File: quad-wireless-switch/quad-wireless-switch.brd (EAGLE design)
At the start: 38.1 x 108 mm, 78 parts, among them IC1 LM2937IMP-3.3, Q1 DN2625K4-G, Q2 SI2323DS-T1-E3, Q3 IRL520, Q4 IRL520, Q5 IRL520, Q6 IRL520, U2 SDB501

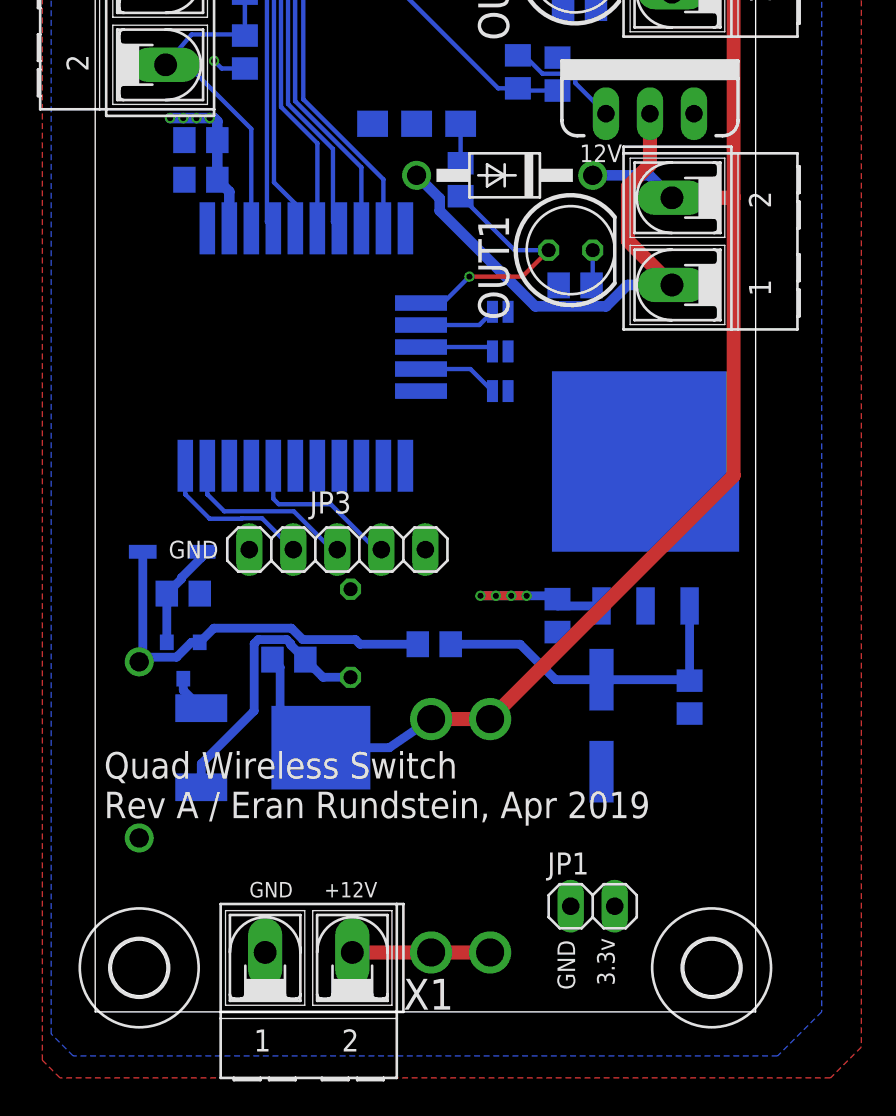
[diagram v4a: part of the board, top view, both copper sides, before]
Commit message: quad-wireless-switch
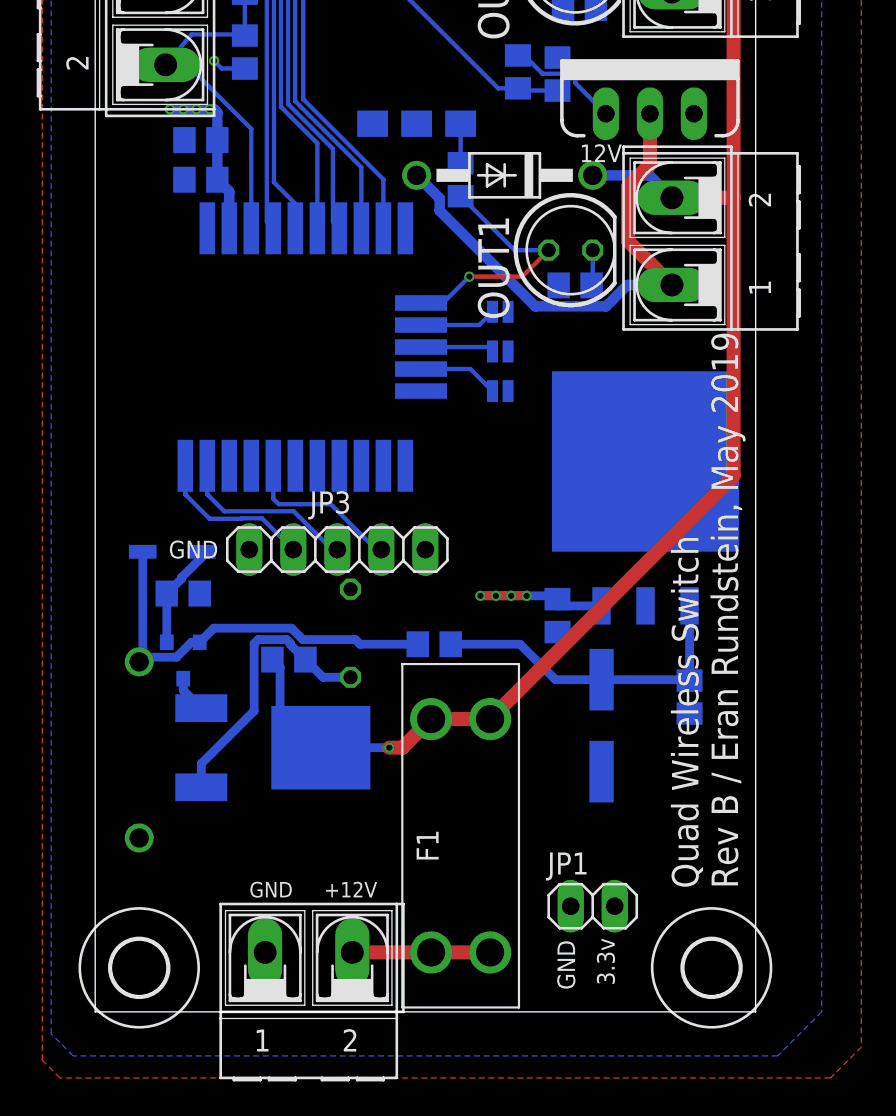
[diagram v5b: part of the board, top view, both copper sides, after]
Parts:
- flipped F1 to the top
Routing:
- net 3.3V: track 27.6 -> 28.1 mm
- net 12V: track 167.2 -> 167.4 mm, vias 3 -> 4
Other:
- board text added: "Quad Wireless Switch Rev B / Eran Rundstein, May 2019"
- board text removed: "Quad Wireless Switch Rev A / Eran Rundstein, Apr 2019"
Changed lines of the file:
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@@
 <wire x1="38.1" y1="107.95" x2="0" y2="107.95" width="0" layer="20"/>
 <wire x1="0" y1="107.95" x2="0" y2="0" width="0" layer="20"/>
-<text x="0.508" y="11.176" size="1.524" layer="25">Quad Wireless Switch
-Rev A / Eran Rundstein, Apr 2019</text>
+<text x="37.084" y="7.112" size="1.524" layer="25" rot="R90">Quad Wireless Switch
+Rev B / Eran Rundstein, May 2019</text>
 <text x="13.208" y="6.604" size="0.889" layer="25">+12V</text>
 <text x="8.89" y="6.604" size="0.889" layer="25">GND</text>
@@
 <attribute name="MF" value="" x="12.319" y="3.429" size="1.778" layer="27" display="off"/>
 <attribute name="MPN" value="" x="12.319" y="3.429" size="1.778" layer="27" display="off"/>
-<attribute name="NAME" x="17.78" y="0.127" size="1.778" layer="25"/>
 <attribute name="OC_FARNELL" value="unknown" x="12.319" y="3.429" size="1.778" layer="27" display="off"/>
 <attribute name="OC_NEWARK" value="unknown" x="12.319" y="3.429" size="1.778" layer="27" display="off"/>
 <attribute name="VALUE" x="9.144" y="-2.286" size="1.778" layer="27"/>
 </element>
-<element name="F1" library="keves-ng" library_urn="urn:adsk.eagle:library:1429743" package="KEYSTONE-3557-2" package3d_urn="urn:adsk.eagle:package:1429787/2" value="KEYSTONE-3557-2" x="21.082" y="10.16" smashed="yes" rot="MR90">
-<attribute name="NAME" x="22.352" y="8.636" size="1.27" layer="26" rot="MR90"/>
+<element name="F1" library="keves-ng" library_urn="urn:adsk.eagle:library:1429743" package="KEYSTONE-3557-2" package3d_urn="urn:adsk.eagle:package:1429787/2" value="KEYSTONE-3557-2" x="21.082" y="10.16" smashed="yes" rot="R90">
+<attribute name="NAME" x="19.812" y="8.636" size="1.27" layer="25" rot="R90"/>
 </element>
 <element name="Q1" library="SparkFun-DiscreteSemi" package="DPAK" value="DN2625K4-G" x="11.43" y="15.24" smashed="yes" rot="MR90">
@@
 <wire x1="7.736" y1="47.316" x2="7.046" y2="48.006" width="0.6096" layer="16"/>
 <wire x1="7.046" y1="48.006" x2="7.046" y2="50.292" width="0.6096" layer="16"/>
-<wire x1="7.046" y1="50.292" x2="7.046" y2="51.374" width="0.6096" layer="16"/>
-<wire x1="7.046" y1="51.374" x2="6.858" y2="51.562" width="0.6096" layer="16"/>
-<wire x1="6.858" y1="51.562" x2="6.604" y2="51.562" width="0.6096" layer="16"/>
-<wire x1="6.604" y1="51.562" x2="5.842" y2="51.562" width="0.6096" layer="16"/>
-<wire x1="5.842" y1="51.562" x2="5.08" y2="51.562" width="0.6096" layer="16"/>
-<wire x1="5.08" y1="51.562" x2="4.318" y2="51.562" width="0.6096" layer="16"/>
-<via x="4.318" y="51.562" extent="1-16" drill="0.35"/>
-<via x="5.08" y="51.562" extent="1-16" drill="0.35"/>
-<via x="5.842" y="51.562" extent="1-16" drill="0.35"/>
-<via x="6.604" y="51.562" extent="1-16" drill="0.35"/>
+<wire x1="7.046" y1="50.292" x2="7.046" y2="51.882" width="0.6096" layer="16"/>
+<wire x1="7.046" y1="51.882" x2="6.858" y2="52.07" width="0.6096" layer="16"/>
+<wire x1="6.858" y1="52.07" x2="6.604" y2="52.07" width="0.6096" layer="16"/>
+<wire x1="6.604" y1="52.07" x2="5.842" y2="52.07" width="0.6096" layer="16"/>
+<wire x1="5.842" y1="52.07" x2="5.08" y2="52.07" width="0.6096" layer="16"/>
+<wire x1="5.08" y1="52.07" x2="4.318" y2="52.07" width="0.6096" layer="16"/>
+<via x="4.318" y="52.07" extent="1-16" drill="0.35"/>
+<via x="5.08" y="52.07" extent="1-16" drill="0.35"/>
+<via x="5.842" y="52.07" extent="1-16" drill="0.35"/>
+<via x="6.604" y="52.07" extent="1-16" drill="0.35"/>
 <contactref element="JP1" pad="2"/>
 </signal>
@@
 <contactref element="R1" pad="2"/>
 <contactref element="OUT1" pad="2"/>
-<wire x1="19.3802" y1="16.891" x2="16.9672" y2="15.24" width="0.508" layer="16"/>
 <wire x1="16.9672" y1="15.24" x2="13.018" y2="15.24" width="0.508" layer="16"/>
 <wire x1="10.226" y1="20.32" x2="10.668" y2="19.878" width="0.508" layer="16"/>
 <wire x1="10.668" y1="19.878" x2="10.668" y2="15.24" width="0.508" layer="16"/>
 <wire x1="10.668" y1="15.24" x2="13.018" y2="15.24" width="0.508" layer="16"/>
-<wire x1="19.3802" y1="16.891" x2="22.7838" y2="16.891" width="0.8128" layer="1"/>
-<wire x1="22.7838" y1="16.891" x2="36.83" y2="30.9372" width="0.8128" layer="1"/>
 <wire x1="36.83" y1="30.9372" x2="36.83" y2="46.99" width="0.8128" layer="1"/>
 <wire x1="36.83" y1="46.99" x2="36.83" y2="63.754" width="0.8128" layer="1"/>
@@
 <wire x1="21.778" y1="100.33" x2="26.416" y2="100.33" width="0.254" layer="16"/>
 <wire x1="26.416" y1="100.33" x2="28.956" y2="97.79" width="0.254" layer="16"/>
+<via x="16.9672" y="15.24" extent="1-16" drill="0.35"/>
+<wire x1="36.83" y1="30.9372" x2="22.7838" y2="16.891" width="0.8128" layer="1"/>
+<wire x1="22.7838" y1="16.891" x2="19.3802" y2="16.891" width="0.8128" layer="1"/>
+<wire x1="16.9672" y1="15.24" x2="17.7292" y2="15.24" width="0.8128" layer="1"/>
+<wire x1="17.7292" y1="15.24" x2="19.3802" y2="16.891" width="0.8128" layer="1"/>
 </signal>
 <signal name="N$6">
@@
 <contactref element="F1" pad="L2"/>
 <contactref element="X1" pad="2"/>
-<wire x1="14.8336" y1="3.429" x2="19.3802" y2="3.429" width="0.8128" layer="1"/>
-<wire x1="19.3802" y1="3.429" x2="22.7838" y2="3.429" width="0.8128" layer="1"/>
+<wire x1="22.7838" y1="3.429" x2="19.3802" y2="3.429" width="0.8128" layer="1"/>
+<wire x1="19.3802" y1="3.429" x2="14.8336" y2="3.429" width="0.8128" layer="1"/>
 </signal>
 <signal name="N$21">
